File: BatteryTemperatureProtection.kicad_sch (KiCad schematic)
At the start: 5 parts, among them U11 BTS5090-1EJA

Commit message: First pass at new schematics and board
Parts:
- added C18: 10uF, Capacitor_SMD:C_0805_2012Metric, symbol Device:C_Small
- R27: footprint (none) -> Resistor_SMD:R_0603_1608Metric
- R40, R41, R42: footprint (none) -> Resistor_SMD:R_2010_5025Metric
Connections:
- net GND: now also C18.2
- net SYSTEM_VDD: now also C18.1
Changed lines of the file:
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@@
+	(wire
+		(pts
+			(xy 113.03 67.31) (xy 113.03 71.12)
+		)
+		(stroke
+			(width 0)
+			(type default)
+		)
+	)
 	(wire
 		(pts
@@
 		(pts
 			(xy 177.8 99.06) (xy 184.15 99.06)
+		)
+		(stroke
+			(width 0)
+			(type default)
+		)
+	)
+	(wire
+		(pts
+			(xy 113.03 76.2) (xy 113.03 80.01)
 		)
 		(stroke
@@
 			)
 		)
-		(property "Footprint" ""
+		(property "Footprint" "Resistor_SMD:R_2010_5025Metric"
 			(at 186.69 114.3 0)
 			(effects
@@
 	(symbol
 		(lib_id "power:+1V0")
+		(at 113.03 67.31 0)
+		(unit 1)
+		(exclude_from_sim no)
+		(in_bom yes)
+		(on_board yes)
+		(dnp no)
+		(property "Reference" "#PWR039"
+			(at 113.03 71.12 0)
+			(effects
+				(font
+					(size 1.27 1.27)
+				)
+				(hide yes)
+			)
+		)
+		(property "Value" "SYSTEM_VDD"
+			(at 113.03 62.23 0)
+			(effects
+				(font
+					(size 1.27 1.27)
+				)
+			)
+		)
+		(property "Footprint" ""
+			(at 113.03 67.31 0)
+			(effects
+				(font
+					(size 1.27 1.27)
+				)
+				(hide yes)
+			)
+		)
+		(property "Datasheet" ""
+			(at 113.03 67.31 0)
+			(effects
+				(font
+					(size 1.27 1.27)
+				)
+				(hide yes)
+			)
+		)
+		(property "Description" "Power symbol creates a global label with name \"+1V0\""
+			(at 113.03 67.31 0)
+			(effects
+				(font
+					(size 1.27 1.27)
+				)
+				(hide yes)
+			)
+		)
+		(pin "1"
+		)
+		(instances
+			(project "BatteryBoard"
+				(path "/b6fd875d-6e05-4440-9a05-0f0aa046a0ef/8b9e55cd-928e-4578-a188-133f4642b05f"
+					(reference "#PWR039")
+					(unit 1)
+				)
+				(path "/b6fd875d-6e05-4440-9a05-0f0aa046a0ef/b0261011-2adb-4b34-9815-14af15ff5ea4"
+					(reference "#PWR040")
+					(unit 1)
+				)
+			)
+		)
+	)
+	(symbol
+		(lib_id "power:+1V0")
 		(at 139.7 86.36 0)
 		(unit 1)
@@
 		(dnp no)
 		(fields_autoplaced yes)
-		(property "Reference" "#PWR026"
+		(property "Reference" "#PWR0101"
 			(at 139.7 90.17 0)
 			(effects
@@
 		(instances
 			(project "BatteryBoard"
+				(path "/b6fd875d-6e05-4440-9a05-0f0aa046a0ef/8b9e55cd-928e-4578-a188-133f4642b05f"
+					(reference "#PWR0101")
+					(unit 1)
+				)
 				(path "/b6fd875d-6e05-4440-9a05-0f0aa046a0ef/b0261011-2adb-4b34-9815-14af15ff5ea4"
 					(reference "#PWR026")
@@
 	)
 	(symbol
+		(lib_id "Device:C_Small")
+		(at 113.03 73.66 0)
+		(unit 1)
+		(exclude_from_sim no)
+		(in_bom yes)
+		(on_board yes)
+		(dnp no)
+		(fields_autoplaced yes)
+		(property "Reference" "C18"
+			(at 115.57 72.3962 0)
+			(effects
+				(font
+					(size 1.27 1.27)
+				)
+				(justify left)
+			)
+		)
+		(property "Value" "10uF"
+			(at 115.57 74.9362 0)
+			(effects
+				(font
+					(size 1.27 1.27)
+				)
+				(justify left)
+			)
+		)
+		(property "Footprint" "Capacitor_SMD:C_0805_2012Metric"
+			(at 113.03 73.66 0)
+			(effects
+				(font
+					(size 1.27 1.27)
+				)
+				(hide yes)
+			)
+		)
+		(property "Datasheet" "~"
+			(at 113.03 73.66 0)
+			(effects
+				(font
+					(size 1.27 1.27)
+				)
+				(hide yes)
+			)
+		)
+		(property "Description" "Unpolarized capacitor, small symbol"
+			(at 113.03 73.66 0)
+			(effects
+				(font
+					(size 1.27 1.27)
+				)
+				(hide yes)
+			)
+		)
+		(pin "1"
+		)
+		(pin "2"
+		)
+		(instances
+			(project ""
+				(path "/b6fd875d-6e05-4440-9a05-0f0aa046a0ef/8b9e55cd-928e-4578-a188-133f4642b05f"
+					(reference "C18")
+					(unit 1)
+				)
+				(path "/b6fd875d-6e05-4440-9a05-0f0aa046a0ef/b0261011-2adb-4b34-9815-14af15ff5ea4"
+					(reference "C19")
+					(unit 1)
+				)
+			)
+		)
+	)
+	(symbol
+		(lib_id "power:GND")
+		(at 113.03 80.01 0)
+		(unit 1)
+		(exclude_from_sim no)
+		(in_bom yes)
+		(on_board yes)
+		(dnp no)
+		(fields_autoplaced yes)
+		(property "Reference" "#PWR041"
+			(at 113.03 86.36 0)
+			(effects
+				(font
+					(size 1.27 1.27)
+				)
+				(hide yes)
+			)
+		)
+		(property "Value" "GND"
+			(at 113.03 85.09 0)
+			(effects
+				(font
+					(size 1.27 1.27)
+				)
+			)
+		)
+		(property "Footprint" ""
+			(at 113.03 80.01 0)
+			(effects
+				(font
+					(size 1.27 1.27)
+				)
+				(hide yes)
+			)
+		)
+		(property "Datasheet" ""
+			(at 113.03 80.01 0)
+			(effects
+				(font
+					(size 1.27 1.27)
+				)
+				(hide yes)
+			)
+		)
+		(property "Description" "Power symbol creates a global label with name \"GND\" , ground"
+			(at 113.03 80.01 0)
+			(effects
+				(font
+					(size 1.27 1.27)
+				)
+				(hide yes)
+			)
+		)
+		(pin "1"
+		)
+		(instances
+			(project "BatteryBoard"
+				(path "/b6fd875d-6e05-4440-9a05-0f0aa046a0ef/8b9e55cd-928e-4578-a188-133f4642b05f"
+					(reference "#PWR041")
+					(unit 1)
+				)
+				(path "/b6fd875d-6e05-4440-9a05-0f0aa046a0ef/b0261011-2adb-4b34-9815-14af15ff5ea4"
+					(reference "#PWR042")
+					(unit 1)
+				)
+			)
+		)
+	)
+	(symbol
 		(lib_id "power:GND")
 		(at 139.7 115.57 0)
@@
 			)
 		)
-		(property "Footprint" ""
+		(property "Footprint" "Resistor_SMD:R_0603_1608Metric"
 			(at 127 106.68 0)
 			(effects
@@
 			)
 		)
-		(property "Footprint" ""
+		(property "Footprint" "Resistor_SMD:R_2010_5025Metric"
 			(at 186.69 99.06 0)
 			(effects
@@
 			)
 		)
-		(property "Footprint" ""
+		(property "Footprint" "Resistor_SMD:R_2010_5025Metric"
 			(at 186.69 106.68 0)
 			(effects

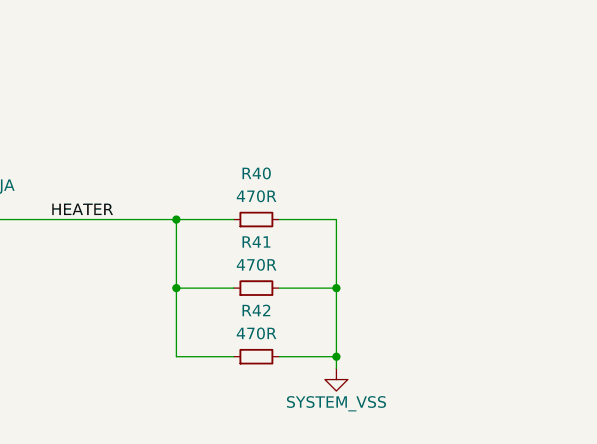
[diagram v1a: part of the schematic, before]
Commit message: Updated footprint to follow PC/104
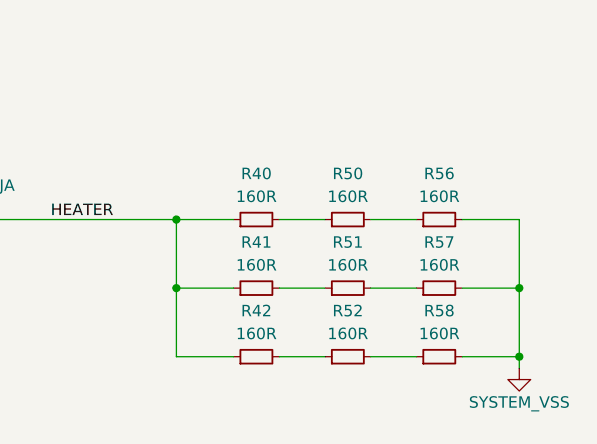
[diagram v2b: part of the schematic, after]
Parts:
- added R50, R51, R52, R56, R57, R58: 160R, Resistor_SMD:R_2010_5025Metric, symbol Device:R_Small
- R40, R41, R42: value 470R -> 160R
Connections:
- net SYSTEM_VSS: now also R56.2, R57.2, R58.2; no longer R40.2, R41.2, R42.2
- new net: R51.2, R57.1
- new net: R42.2, R52.1
- new net: R52.2, R58.1
- new net: R40.2, R50.1
- new net: R50.2, R56.1
- new net: R41.2, R51.1

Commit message: v2.1 (v3?) Partial Updates
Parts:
- removed C18: 10uF, Capacitor_SMD:C_0805_2012Metric, symbol Device:C_Small
- removed R27: 1k, Resistor_SMD:R_0603_1608Metric, symbol Device:R_Small
- removed R40, R41, R42, R50, R51, R52, R56, R57, R58: 160R, Resistor_SMD:R_2010_5025Metric, symbol Device:R_Small
- removed U11: BTS5090-1EJA, Package_SO:Infineon_PG-DSO-8-43, symbol Power_Management:BTS5090-1EJA
- added C5, C6: 1uF, Capacitor_SMD:C_0603_1608Metric, symbol Device:C_Small
- added D3, D4: GREEN, LED_SMD:LED_0603_1608Metric, symbol Device:LED_Small
- added Q1, Q23: IRLML2803, Package_TO_SOT_SMD:SOT-23, symbol Argus-IC:IRLML2803
- added Q2, Q4: SIRA99DP-T1-GE3, Package_SO:PowerPAK_SO-8_Single, symbol Transistor_FET:Si7141DP
- added R10: 100k, Resistor_SMD:R_0603_1608Metric, symbol Device:R_Small
- added R11, R14, R16, R17, R18, R8, R9: 10k, Resistor_SMD:R_0603_1608Metric, symbol Device:R_Small
- added R12: 0.05R, Resistor_SMD:R_1206_3216Metric, symbol Device:R_Small
- added R13: 0R, Resistor_SMD:R_0603_1608Metric, symbol Device:R_Small
- added R15: 30k, Resistor_SMD:R_0603_1608Metric, symbol Device:R_Small
- added R19, R7: 2.7k, Resistor_SMD:R_0603_1608Metric, symbol Device:R_Small
- added U3: MAX4211B/E, Package_DFN_QFN:QFN-16-1EP_4x4mm_P0.65mm_EP2.1x2.1mm, symbol Argus-IC:MAX4211
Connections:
- net GND: now also C5.2, D3.1 (K), D4.1 (K), Q1.2 (S), Q23.2 (S), R10.1, R15.1, R16.1, R8.1, U3.17 (GND), U3.7 (GND), U3.EPAD (GND)
- net SYSTEM_VDD: now also Q4.1 (S), Q4.2 (S), Q4.3 (S), R9.2
- new net: D3.2 (A), R7.2
- new net: Q23.3 (D), Q4.4 (G), R9.1
- new net: Q1.1 (G), Q2.4 (G), R17.1, U3.3 (LE), U3.4 (COUT1), U3.6 (COUT2)
- new net: Q2.1 (S), Q2.2 (S), Q2.3 (S), R12.2, R17.2, U3.15 (RS-)
- new net: R13.1, U3.10 (CIN1+)
- new net: R14.1, R15.2, U3.11 (CIN1-)
- new net: R14.2, U3.12 (REF), U3.8 (CIN2+)
- new net: R13.2, U3.14 (IOUT)
- new net: Q4.5 (D), R12.1, U3.16 (RS+)
- new net: R11.1, U3.5 (INHIBIT)
- new net: C6.1, R10.2, R11.2
- new net: D4.2 (A), R19.1
- new net +3V3: R18.2
- new net CB-RESET: R16.2, U3.9 (CIN2-)
- new net ON/~{OFF}: C5.1, Q23.1 (G), R7.1, R8.2, U3.1 (VCC)
- new net VBUS: C6.2, Q2.5 (D), R19.2
- new net ~{FAULT}: Q1.3 (D), R18.1
- no-connect marks 0 -> 1
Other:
- added sheet BatteryHeater (BatteryHeater.kicad_sch)
- added sheet BatteryHeater1 (BatteryHeater.kicad_sch)
- note added: "ADD TVS?"
- note added: "A_VIOUT = 16.67 (MAX4211A/D) A_VIOUT = 25.00 (MAX4211B/E) (select) A_VIOUT = 40.96 (MAX4211C/F)"
- note added: "Battery protection design derived from Portland State University's Open-Source OreSat project"
- note added: "V_IOUT Max = VCC - 0.25V = 3.08V V_IOUT = A_VIOUT * V_SENSE V_IOUT = A_VIOUT * (R_SENSE * I_LOAD) V_IOUT = 25 * (0.05 * I_LOAD) For Trip Current, V_IOUT = CIN1- I_LOAD (trip) = 0.9075 / (25 * 0.05) I_LOAD (trip) = 0.726A"
- note added: "V_Ref = 1.21V CIN1- Set to R73 / (R71 + R73) * V_Ref = 0.9075V"
- company: (none) -> Carnegie Mellon University
- title: (none) -> Argus Batteryboard

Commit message: More updates
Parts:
- removed C5, C6: 1uF, Capacitor_SMD:C_0603_1608Metric, symbol Device:C_Small
- removed D3: GREEN, LED_SMD:LED_0603_1608Metric, symbol Device:LED_Small
- removed Q1: IRLML2803, Package_TO_SOT_SMD:SOT-23, symbol Argus-IC:IRLML2803
- removed Q2: SIRA99DP-T1-GE3, Package_SO:PowerPAK_SO-8_Single, symbol Transistor_FET:Si7141DP
- removed R10: 100k, Resistor_SMD:R_0603_1608Metric, symbol Device:R_Small
- removed R11, R14, R16, R17, R18: 10k, Resistor_SMD:R_0603_1608Metric, symbol Device:R_Small
- removed R12: 0.05R, Resistor_SMD:R_1206_3216Metric, symbol Device:R_Small
- removed R13: 0R, Resistor_SMD:R_0603_1608Metric, symbol Device:R_Small
- removed R15: 30k, Resistor_SMD:R_0603_1608Metric, symbol Device:R_Small
- removed U3: MAX4211B/E, Package_DFN_QFN:QFN-16-1EP_4x4mm_P0.65mm_EP2.1x2.1mm, symbol Argus-IC:MAX4211
- R7: value 2.7k -> 1k
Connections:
- net VBUS: now also Q4.5 (D)
- net HEATER_ENABLE: now reaches R7.2
- net HEATER_ENABLE: now also R8.2
- net ON/~{OFF}: no longer names the net of Q23.1 (G), R7.1
- net ON/~{OFF}: no longer R8.2
- no-connect marks 1 -> 0
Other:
- note removed: "ADD TVS?"
- note removed: "A_VIOUT = 16.67 (MAX4211A/D) A_VIOUT = 25.00 (MAX4211B/E) (select) A_VIOUT = 40.96 (MAX4211C/F)"
- note removed: "Battery protection design derived from Portland State University's Open-Source OreSat project"
- note removed: "V_IOUT Max = VCC - 0.25V = 3.08V V_IOUT = A_VIOUT * V_SENSE V_IOUT = A_VIOUT * (R_SENSE * I_LOAD) V_IOUT = 25 * (0.05 * I_LOAD) For Trip Current, V_IOUT = CIN1- I_LOAD (trip) = 0.9075 / (25 * 0.05) I_LOAD (trip) = 0.726A"
- note removed: "V_Ref = 1.21V CIN1- Set to R73 / (R71 + R73) * V_Ref = 0.9075V"
- moved on the sheet: D4, Q23, Q4, R19, R8, R9

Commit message: Finalized updates with recommendations and exported files
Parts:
- added F9: 5A, Fuse:Fuse_1206_3216Metric, symbol Device:Fuse_Small
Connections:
- net SYSTEM_VDD: now also F9.2; no longer Q4.1 (S), Q4.2 (S), Q4.3 (S), R9.2
- new net: F9.1, Q4.1 (S), Q4.2 (S), Q4.3 (S), R9.2
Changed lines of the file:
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@@
+	(wire
+		(pts
+			(xy 133.35 77.47) (xy 133.35 80.01)
+		)
+		(stroke
+			(width 0)
+			(type default)
+		)
+	)
 	(wire
 		(pts
@@
 	(wire
 		(pts
-			(xy 162.56 80.01) (xy 162.56 87.63)
+			(xy 162.56 77.47) (xy 162.56 87.63)
 		)
 		(stroke
@@
 	(wire
 		(pts
-			(xy 133.35 80.01) (xy 133.35 87.63)
-		)
-		(stroke
-			(width 0.1524)
-			(type solid)
-		)
-	)
-	(wire
-		(pts
 			(xy 133.35 97.79) (xy 147.32 97.79)
 		)
@@
 		(pts
 			(xy 147.32 97.79) (xy 147.32 95.25)
+		)
+		(stroke
+			(width 0.1524)
+			(type solid)
+		)
+	)
+	(wire
+		(pts
+			(xy 133.35 85.09) (xy 133.35 87.63)
 		)
 		(stroke
@@
 		(shape input)
 		(at 106.68 191.77 180)
-		(fields_autoplaced yes)
 		(effects
 			(font
@@
 		(shape input)
 		(at 106.68 181.61 180)
-		(fields_autoplaced yes)
 		(effects
 			(font
@@
 		(shape input)
 		(at 100.33 105.41 180)
-		(fields_autoplaced yes)
 		(effects
 			(font
@@
 	(symbol
 		(lib_id "power:+1V0")
-		(at 133.35 80.01 0)
+		(at 133.35 77.47 0)
 		(unit 1)
 		(exclude_from_sim no)
@@
 		(dnp no)
 		(property "Reference" "#PWR022"
-			(at 133.35 83.82 0)
+			(at 133.35 81.28 0)
 			(effects
 				(font
@@
 		)
 		(property "Value" "SYSTEM_VDD"
-			(at 133.35 75.946 0)
+			(at 133.35 73.406 0)
 			(effects
 				(font
@@
 		)
 		(property "Footprint" ""
-			(at 133.35 80.01 0)
+			(at 133.35 77.47 0)
 			(effects
 				(font
@@
 		)
 		(property "Datasheet" ""
-			(at 133.35 80.01 0)
+			(at 133.35 77.47 0)
 			(effects
 				(font
@@
 		)
 		(property "Description" "Power symbol creates a global label with name \"+1V0\""
-			(at 133.35 80.01 0)
+			(at 133.35 77.47 0)
 			(effects
 				(font
@@
 	)
 	(symbol
+		(lib_id "Device:Fuse_Small")
+		(at 133.35 82.55 90)
+		(unit 1)
+		(exclude_from_sim no)
+		(in_bom yes)
+		(on_board yes)
+		(dnp no)
+		(property "Reference" "F9"
+			(at 131.826 81.5341 90)
+			(effects
+				(font
+					(size 1.27 1.27)
+				)
+				(justify left)
+			)
+		)
+		(property "Value" "5A"
+			(at 131.826 83.566 90)
+			(effects
+				(font
+					(size 1.27 1.27)
+				)
+				(justify left)
+			)
+		)
+		(property "Footprint" "Fuse:Fuse_1206_3216Metric"
+			(at 133.35 82.55 0)
+			(effects
+				(font
+					(size 1.27 1.27)
+				)
+				(hide yes)
+			)
+		)
+		(property "Datasheet" "~"
+			(at 133.35 82.55 0)
+			(effects
+				(font
+					(size 1.27 1.27)
+				)
+				(hide yes)
+			)
+		)
+		(property "Description" "Fuse, small symbol"
+			(at 133.35 82.55 0)
+			(effects
+				(font
+					(size 1.27 1.27)
+				)
+				(hide yes)
+			)
+		)
+		(pin "1"
+		)
+		(pin "2"
+		)
+		(instances
+			(project ""
+				(path "/b6fd875d-6e05-4440-9a05-0f0aa046a0ef/8b9e55cd-928e-4578-a188-133f4642b05f"
+					(reference "F9")
+					(unit 1)
+				)
+			)
+		)
+	)
+	(symbol
 		(lib_id "Device:R_Small")
 		(at 162.56 95.25 180)
@@
 	(symbol
 		(lib_id "power:VBUS")
-		(at 162.56 80.01 0)
+		(at 162.56 77.47 0)
 		(unit 1)
 		(exclude_from_sim no)
@@
 		(dnp no)
 		(property "Reference" "#PWR058"
-			(at 162.56 83.82 0)
+			(at 162.56 81.28 0)
 			(effects
 				(font
@@
 		)
 		(property "Value" "VBUS"
-			(at 162.56 76.454 0)
+			(at 162.56 73.914 0)
 			(effects
 				(font
@@
 		)
 		(property "Footprint" ""
-			(at 162.56 80.01 0)
+			(at 162.56 77.47 0)
 			(effects
 				(font
@@
 		)
 		(property "Datasheet" ""
-			(at 162.56 80.01 0)
+			(at 162.56 77.47 0)
 			(effects
 				(font
@@
 		)
 		(property "Description" "Power symbol creates a global label with name \"VBUS\""
-			(at 162.56 80.01 0)
-			(effects
-				(font
+			(at 162.56 77.47 0)
+			(effects
+				(font

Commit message: v3.1 Updates
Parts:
- R10: renamed from R19; value 2.7k -> 10k
- renumbered D4 to D3, Q4 to Q1, Q23 to Q2, R8 to R7, R7 to R8
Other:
- moved on the sheet: R9
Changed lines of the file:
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@@
 		(on_board yes)
 		(dnp no)
-		(property "Reference" "R7"
-			(at 119.38 101.092 90)
+		(property "Reference" "R8"
+			(at 119.38 101.6 90)
 			(effects
 				(font
@@
 		)
 		(property "Value" "1k"
-			(at 119.38 103.124 90)
+			(at 119.38 103.378 90)
 			(effects
 				(font
@@
 			(project "Avionics-BatteryBoard"
 				(path "/b6fd875d-6e05-4440-9a05-0f0aa046a0ef/8b9e55cd-928e-4578-a188-133f4642b05f"
-					(reference "R7")
+					(reference "R8")
 					(unit 1)
 				)
@@
 		(on_board yes)
 		(dnp no)
-		(property "Reference" "R8"
-			(at 115.57 109.982 0)
-			(effects
-				(font
-					(size 1.27 1.27)
-				)
-				(justify left bottom)
+		(property "Reference" "R7"
+			(at 113.03 110.744 0)
+			(effects
+				(font
+					(size 1.27 1.27)
+				)
+				(justify right)
 			)
 		)
 		(property "Value" "10k"
-			(at 116.586 112.014 0)
-			(effects
-				(font
-					(size 1.27 1.27)
-				)
-				(justify left bottom)
+			(at 113.03 112.776 0)
+			(effects
+				(font
+					(size 1.27 1.27)
+				)
+				(justify right)
 			)
 		)
@@
 			(project "BatteryBoard"
 				(path "/b6fd875d-6e05-4440-9a05-0f0aa046a0ef/8b9e55cd-928e-4578-a188-133f4642b05f"
-					(reference "R8")
+					(reference "R7")
 					(unit 1)
 				)
@@
 		(on_board yes)
 		(dnp no)
-		(property "Reference" "Q23"
+		(property "Reference" "Q2"
 			(at 135.89 104.14 0)
 			(effects
@@
 			(project "BatteryBoard"
 				(path "/b6fd875d-6e05-4440-9a05-0f0aa046a0ef/8b9e55cd-928e-4578-a188-133f4642b05f"
-					(reference "Q23")
+					(reference "Q2")
 					(unit 1)
 				)
@@
 		(on_board yes)
 		(dnp no)
-		(property "Reference" "Q4"
+		(property "Reference" "Q1"
 			(at 147.32 81.28 90)
 			(effects
@@
 			(project "BatteryBoard"
 				(path "/b6fd875d-6e05-4440-9a05-0f0aa046a0ef/8b9e55cd-928e-4578-a188-133f4642b05f"
-					(reference "Q4")
+					(reference "Q1")
 					(unit 1)
 				)
@@
 		(dnp no)
 		(property "Reference" "F9"
-			(at 131.826 81.5341 90)
+			(at 132.334 81.5341 90)
 			(effects
 				(font
@@
 		)
 		(property "Value" "5A"
-			(at 131.826 83.566 90)
+			(at 132.334 83.566 90)
 			(effects
 				(font
@@
 		(on_board yes)
 		(dnp no)
-		(property "Reference" "R19"
-			(at 167.894 93.472 0)
-			(effects
-				(font
-					(size 1.27 1.27)
-				)
-				(justify left bottom)
-			)
-		)
-		(property "Value" "2.7k"
-			(at 168.402 95.504 0)
-			(effects
-				(font
-					(size 1.27 1.27)
-				)
-				(justify left bottom)
+		(property "Reference" "R10"
+			(at 163.83 94.234 0)
+			(effects
+				(font
+					(size 1.27 1.27)
+				)
+				(justify right)
+			)
+		)
+		(property "Value" "10k"
+			(at 163.83 96.266 0)
+			(effects
+				(font
+					(size 1.27 1.27)
+				)
+				(justify right)
 			)
 		)
@@
 			(project "BatteryBoard"
 				(path "/b6fd875d-6e05-4440-9a05-0f0aa046a0ef/8b9e55cd-928e-4578-a188-133f4642b05f"
-					(reference "R19")
+					(reference "R10")
 					(unit 1)
 				)
@@
 	(symbol
 		(lib_id "Device:R_Small")
-		(at 133.35 92.71 180)
+		(at 133.35 92.71 0)
+		(mirror x)
 		(unit 1)
 		(exclude_from_sim no)
@@
 		(dnp no)
 		(property "Reference" "R9"
-			(at 137.16 90.932 0)
-			(effects
-				(font
-					(size 1.27 1.27)
-				)
-				(justify left bottom)
+			(at 132.08 91.694 0)
+			(effects
+				(font
+					(size 1.27 1.27)
+				)
+				(justify right)
 			)
 		)
 		(property "Value" "10k"
-			(at 138.176 92.964 0)
-			(effects
-				(font
-					(size 1.27 1.27)
-				)
-				(justify left bottom)
+			(at 132.08 93.726 0)
+			(effects
+				(font
+					(size 1.27 1.27)
+				)
+				(justify right)
 			)
 		)
@@
 		(on_board yes)
 		(dnp no)
-		(property "Reference" "D4"
-			(at 166.878 102.108 90)
-			(effects
-				(font
-					(size 1.27 1.27)
-				)
-				(justify left bottom)
+		(property "Reference" "D3"
+			(at 164.084 103.124 90)
+			(effects
+				(font
+					(size 1.27 1.27)
+				)
+				(justify right)
 			)
 		)
 		(property "Value" "GREEN"
-			(at 170.434 105.664 90)
-			(effects
-				(font
-					(size 1.27 1.27)
-				)
-				(justify left top)
+			(at 164.084 105.156 90)
+			(effects
+				(font
+					(size 1.27 1.27)
+				)
+				(justify right)
 			)
 		)
@@
 			)
 		)
+		(property "Sim.Pin" "1=K 2=A"
+			(at 162.56 104.14 0)
+			(effects
+				(font
+					(size 1.27 1.27)
+				)
+				(hide yes)
+			)
+		)
 		(pin "1"
 		)
@@
 			(project "BatteryBoard"
 				(path "/b6fd875d-6e05-4440-9a05-0f0aa046a0ef/8b9e55cd-928e-4578-a188-133f4642b05f"
-					(reference "D4")
-					(unit 1)
-				)
+					(reference "D3")
+					(unit 1)
+				)
